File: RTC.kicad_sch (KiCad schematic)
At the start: 3 parts, among them U4 DS3231M

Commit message: Fixed schematic bugs and corresponding layout modifications
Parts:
- U4: value DS3231M -> DS3231S
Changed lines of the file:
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@@
 		)
 	)
-	(hierarchical_label "SDA"
+	(hierarchical_label "SCL"
 		(shape bidirectional)
 		(at 190.5 88.9 0)
@@
 		)
 	)
-	(hierarchical_label "SCL"
+	(hierarchical_label "SDA"
 		(shape bidirectional)
 		(at 190.5 91.44 0)
@@
 			)
 		)
-		(property "Value" "DS3231M"
+		(property "Value" "DS3231S"
 			(at 119.7259 106.68 0)
 			(effects
@@
 		)
 		(pin "SDA_DEVICE" bidirectional
+			(at 154.94 91.44 180)
+			(effects
+				(font
+					(size 1.27 1.27)
+				)
+				(justify left)
+			)
+		)
+		(pin "SCL_DEVICE" bidirectional
 			(at 154.94 88.9 180)
 			(effects
@@
 			)
 		)
-		(pin "SCL_DEVICE" bidirectional
-			(at 154.94 91.44 180)
-			(effects
-				(font
-					(size 1.27 1.27)
-				)
-				(justify left)
-			)
-		)
 		(pin "SDA_BUS" bidirectional
+			(at 180.34 91.44 0)
+			(effects
+				(font
+					(size 1.27 1.27)
+				)
+				(justify right)
+			)
+		)
+		(pin "SCL_BUS" bidirectional
 			(at 180.34 88.9 0)
 			(effects
 				(font
-					(size 1.27 1.27)
-				)
-				(justify right)
-			)
-		)
-		(pin "SCL_BUS" bidirectional
-			(at 180.34 91.44 0)
-			(effects
-				(font

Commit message: Updated version to v2.1
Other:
- company: (none) -> Carnegie Mellon University
- title: (none) -> Argus Mainboard
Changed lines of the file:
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@@
 	(generator_version "8.0")
 	(paper "A4")
+	(title_block
+		(title "Argus Mainboard")
+		(date "2024-11-19")
+		(rev "v2.1")
+		(company "Carnegie Mellon University")
+		(comment 1 "M. Holliday")
+		(comment 2 "N. Khera")
+		(comment 3 "V. Rajesh")
+	)
 	(junction
 		(at 121.92 110.49)

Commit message: v3 partial schematic updates
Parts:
- added F3: 50mA, symbol Device:Fuse_Small
- U4: value DS3231S -> DS3231SN
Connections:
- net +3V3 renamed +3V3_RTC
- net +3V3_RTC: now also F3.2
- new net +3V3_P: F3.1
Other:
- sheet I2C Protection2 ports: added 3V3; removed none
- note added: "0x68"
- note added: "I2C0 ADDR"
- note added: "TODO: Add some way to do full component power cycle"
- moved on the sheet: BT1, C34, U4

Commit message: v3 Layout complete
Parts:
- F2: renamed from F3; footprint (none) -> Fuse:Fuse_0603_1608Metric
- renumbered C34 to C74, U4 to U19
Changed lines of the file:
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@@
 	(title_block
 		(title "Argus Mainboard")
-		(date "2024-11-19")
-		(rev "v2.1")
+		(date "2025-01-08")
+		(rev "v3.0")
 		(company "Carnegie Mellon University")
 		(comment 1 "M. Holliday")
@@
 	(label "RTC_SDA"
 		(at 158.75 91.44 0)
-		(fields_autoplaced yes)
 		(effects
 			(font
@@
 	(label "RTC_SCL"
 		(at 158.75 88.9 0)
-		(fields_autoplaced yes)
 		(effects
 			(font
@@
 		(shape bidirectional)
 		(at 203.2 88.9 0)
-		(fields_autoplaced yes)
 		(effects
 			(font
@@
 		(shape bidirectional)
 		(at 203.2 91.44 0)
-		(fields_autoplaced yes)
 		(effects
 			(font
@@
 		(on_board yes)
 		(dnp no)
-		(property "Reference" "F3"
+		(property "Reference" "F2"
 			(at 152.4 74.422 0)
 			(effects
@@
 			)
 		)
-		(property "Footprint" ""
+		(property "Footprint" "Fuse:Fuse_0603_1608Metric"
 			(at 152.4 76.2 0)
 			(effects
@@
 			(project ""
 				(path "/4c932743-8c6f-426e-9c1f-5a3f2b32c70d/b16b096c-e757-42e7-a323-f6a3422bc211"
-					(reference "F3")
+					(reference "F2")
 					(unit 1)
 				)
@@
 		(on_board yes)
 		(dnp no)
-		(property "Reference" "U4"
-			(at 135.636 85.09 0)
-			(effects
-				(font
-					(size 1.27 1.27)
-				)
-				(justify left)
+		(property "Reference" "U19"
+			(at 133.096 84.836 0)
+			(effects
+				(font
+					(size 1.27 1.27)
+				)
+				(justify right)
 			)
 		)
@@
 			(project "Avionics-MainBoard"
 				(path "/4c932743-8c6f-426e-9c1f-5a3f2b32c70d/b16b096c-e757-42e7-a323-f6a3422bc211"
-					(reference "U4")
+					(reference "U19")
 					(unit 1)
 				)
@@
 		(on_board yes)
 		(dnp no)
-		(property "Reference" "C34"
+		(property "Reference" "C74"
 			(at 103.886 92.964 0)
 			(effects
@@
 			(project "Avionics-MainBoard"
 				(path "/4c932743-8c6f-426e-9c1f-5a3f2b32c70d/b16b096c-e757-42e7-a323-f6a3422bc211"
-					(reference "C34")
+					(reference "C74")
 					(unit 1)
 				)

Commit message: Addressed design issues
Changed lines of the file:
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@@
 	(text "TODO: Add some way to do full component power cycle"
 		(exclude_from_sim no)
-		(at 145.542 130.556 0)
+		(at 149.86 129.032 0)
 		(effects
 			(font

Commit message: v4.0 Updates
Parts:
- renumbered C74 to C72, U19 to U17
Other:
- sheet I2C Protection2 renamed I2C Protection3
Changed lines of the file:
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@@
 (kicad_sch
-	(version 20231120)
+	(version 20250114)
 	(generator "eeschema")
-	(generator_version "8.0")
+	(generator_version "9.0")
 	(paper "A4")
 	(title_block
@@
 		(comment 3 "V. Rajesh")
 	)
+	(text "I2C0 ADDR"
+		(exclude_from_sim no)
+		(at 189.992 105.156 0)
+		(effects
+			(font
+				(size 2.159 2.159)
+			)
+			(justify right bottom)
+		)
+	)
+	(text "0x68"
+		(exclude_from_sim no)
+		(at 180.594 108.458 0)
+		(effects
+			(font
+				(size 2.159 2.159)
+			)
+			(justify right bottom)
+		)
+	)
+	(text "TODO: Add some way to do full component power cycle"
+		(exclude_from_sim no)
+		(at 149.86 129.032 0)
+		(effects
+			(font
+				(size 2.54 2.54)
+			)
+		)
+	)
 	(junction
 		(at 143.51 107.95)
@@
 			(width 0)
 			(type default)
-		)
-	)
-	(text "I2C0 ADDR"
-		(exclude_from_sim no)
-		(at 189.992 105.156 0)
-		(effects
-			(font
-				(size 2.159 2.159)
-			)
-			(justify right bottom)
-		)
-	)
-	(text "0x68"
-		(exclude_from_sim no)
-		(at 180.594 108.458 0)
-		(effects
-			(font
-				(size 2.159 2.159)
-			)
-			(justify right bottom)
-		)
-	)
-	(text "TODO: Add some way to do full component power cycle"
-		(exclude_from_sim no)
-		(at 149.86 129.032 0)
-		(effects
-			(font
-				(size 2.54 2.54)
-			)
 		)
 	)
@@
 		(on_board yes)
 		(dnp no)
-		(property "Reference" "U19"
+		(property "Reference" "U17"
 			(at 133.096 84.836 0)
 			(effects
@@
 			(project "Avionics-MainBoard"
 				(path "/4c932743-8c6f-426e-9c1f-5a3f2b32c70d/b16b096c-e757-42e7-a323-f6a3422bc211"
-					(reference "U19")
+					(reference "U17")
 					(unit 1)
 				)
@@
 		(on_board yes)
 		(dnp no)
-		(property "Reference" "C74"
+		(property "Reference" "C72"
 			(at 103.886 92.964 0)
 			(effects
@@
 			(project "Avionics-MainBoard"
 				(path "/4c932743-8c6f-426e-9c1f-5a3f2b32c70d/b16b096c-e757-42e7-a323-f6a3422bc211"
-					(reference "C74")
+					(reference "C72")
 					(unit 1)
 				)
@@
 		(at 172.72 83.82)
 		(size 25.4 10.16)
+		(exclude_from_sim no)
+		(in_bom yes)
+		(on_board yes)
+		(dnp no)
 		(fields_autoplaced yes)
 		(stroke
@@
 			(color 0 0 0 0.0000)
 		)
-		(property "Sheetname" "I2C Protection2"
+		(property "Sheetname" "I2C Protection3"
 			(at 172.72 83.1084 0)
 			(effects

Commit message: DFM updates
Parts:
- BT1: MPN (none) -> C5189234
- C72: MPN (none) -> C307348
- U17: MPN (none) -> C9866
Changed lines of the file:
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@@
+			)
+		)
+		(property "MPN" "C9866"
+			(at 143.51 93.98 0)
+			(effects
+				(font
+					(size 1.27 1.27)
+				)
+				(hide yes)
 			)
 		)
@@
 			)
 		)
+		(property "MPN" "C5189234"
+			(at 121.92 95.25 0)
+			(effects
+				(font
+					(size 1.27 1.27)
+				)
+				(hide yes)
+			)
+		)
 		(pin "1"
 		)
@@
 			(at 101.6 93.98 0)
 			(effects
+				(font
+					(size 1.27 1.27)
+				)
+				(hide yes)
+			)
+		)
+		(property "MPN" "C307348"
+			(at 101.6 93.98 0)
+			(effects

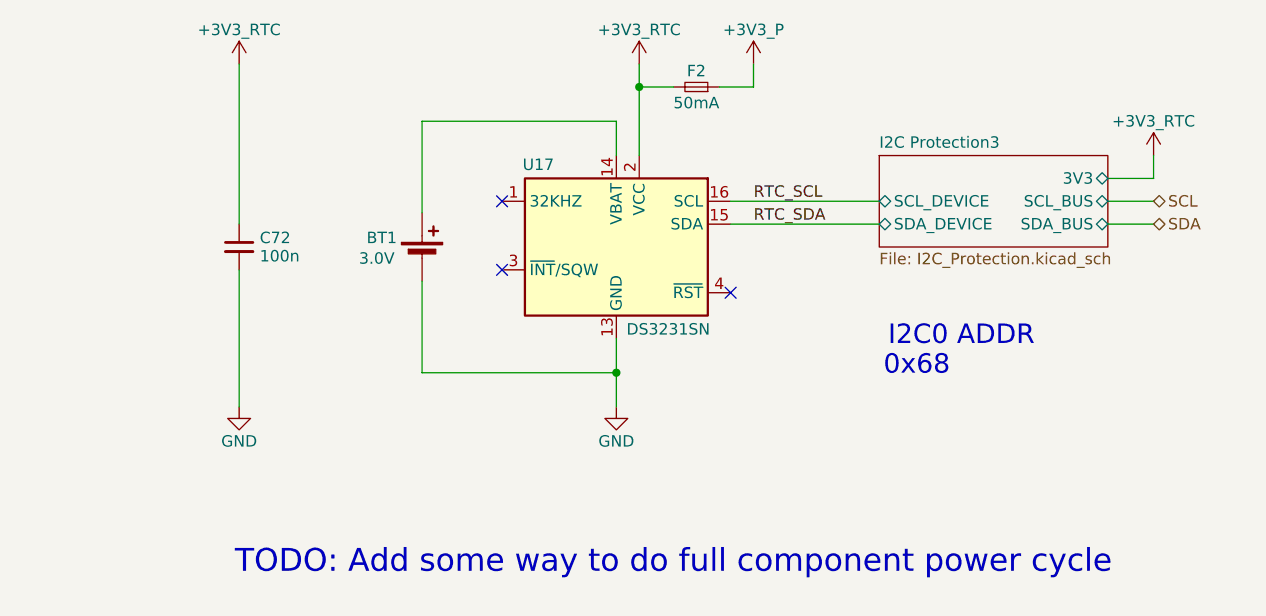
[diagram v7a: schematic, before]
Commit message: Fixed Jetson FPC pinout
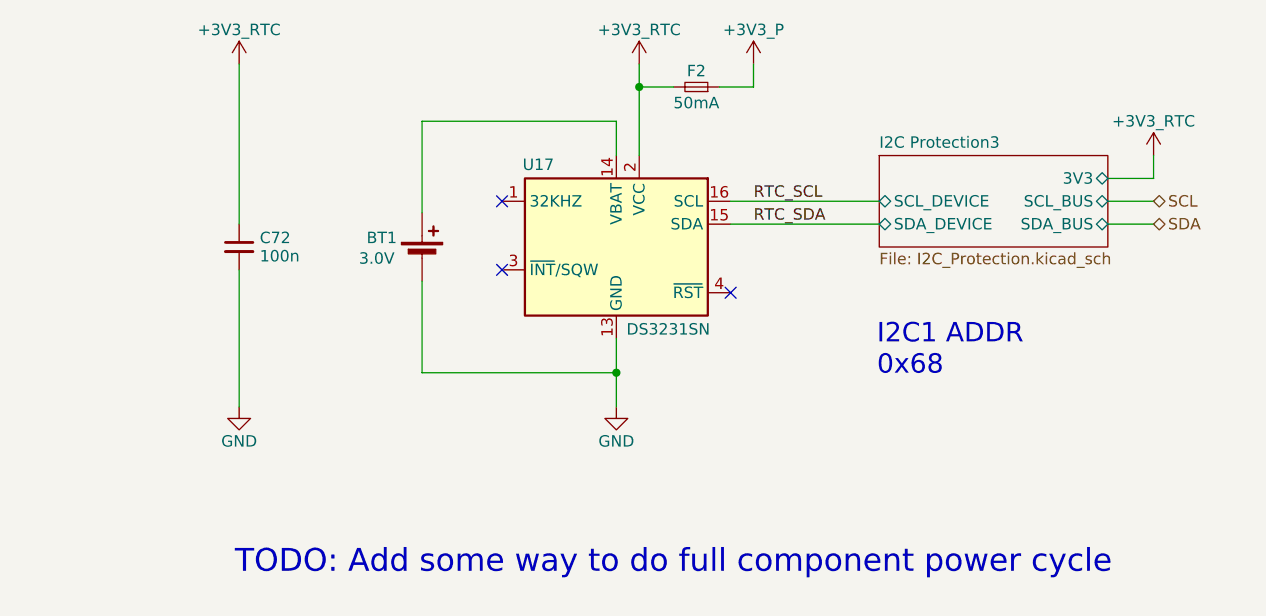
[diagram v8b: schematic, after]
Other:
- note added: "I2C1 ADDR 0x68"
- note removed: "0x68"
- note removed: "I2C0 ADDR"
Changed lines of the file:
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@@
 		(comment 3 "V. Rajesh")
 	)
-	(text "I2C0 ADDR"
+	(text "I2C1 ADDR\n0x68"
 		(exclude_from_sim no)
-		(at 189.992 105.156 0)
+		(at 172.466 108.458 0)
 		(effects
 			(font
 				(size 2.159 2.159)
 			)
-			(justify right bottom)
+			(justify left bottom)
 		)
 	)
-	(text "0x68"
-		(exclude_from_sim no)
-		(at 180.594 108.458 0)
-		(effects
-			(font
-				(size 2.159 2.159)
-			)
-			(justify right bottom)
-		)
-	)
